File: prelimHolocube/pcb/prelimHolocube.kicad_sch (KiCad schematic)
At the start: 43 parts

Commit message: finish pcb
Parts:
- removed C15, C26, C28, C29, C30: 4.7uF, Capacitor_THT:CP_Radial_D4.0mm_P2.00mm, symbol Device:C_US
- removed C25, C27: 1uF, Capacitor_THT:CP_Radial_D5.0mm_P2.50mm, symbol Device:C
- removed R10: 1M, Resistor_THT:R_Axial_DIN0207_L6.3mm_D2.5mm_P7.62mm_Horizontal, symbol Device:R_US
- added C15, C7: 1uF, Capacitor_THT:CP_Radial_D5.0mm_P2.50mm, symbol Device:C
- added C16, C17, C18, C8, C9: 4.7uF, Capacitor_THT:CP_Radial_D4.0mm_P2.00mm, symbol Device:C_US
- added R6: 1M, Resistor_THT:R_Axial_DIN0207_L6.3mm_D2.5mm_P7.62mm_Horizontal, symbol Device:R_US
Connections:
- net +12V: now also C16.1, C8.1
- net +3.3V: now also C15.2, C7.2
- net A06: now also U7.4 (A0); no longer U6.4 (A0)
- net A07: now also U6.4 (A0); no longer U7.4 (A0)
- net CS6: now also U7.6 (CS); no longer U6.6 (CS)
- net CS7: now also U6.6 (CS); no longer U7.6 (CS)
- net GND: now also C15.1, C16.2, C17.2, C18.2, C7.1, C8.2, C9.2, R6.2
- net at C23.1: now also U7.10 (VCOMH); no longer U5.10 (VCOMH)
- net at U5.7 (IREF): now also R6.1; no longer R7.1
- net at R9.1: now also U8.7 (IREF); no longer U6.7 (IREF)
- net at U8.10 (VCOMH): now also C24.1
- net at U6.10 (VCOMH): now also C18.1
- net at U3.10 (VCOMH): now also C9.1; no longer C12.1
- net at U4.10 (VCOMH): now also C12.1
- new net: C17.1, U5.10 (VCOMH)
- new net: R7.1, U6.7 (IREF)

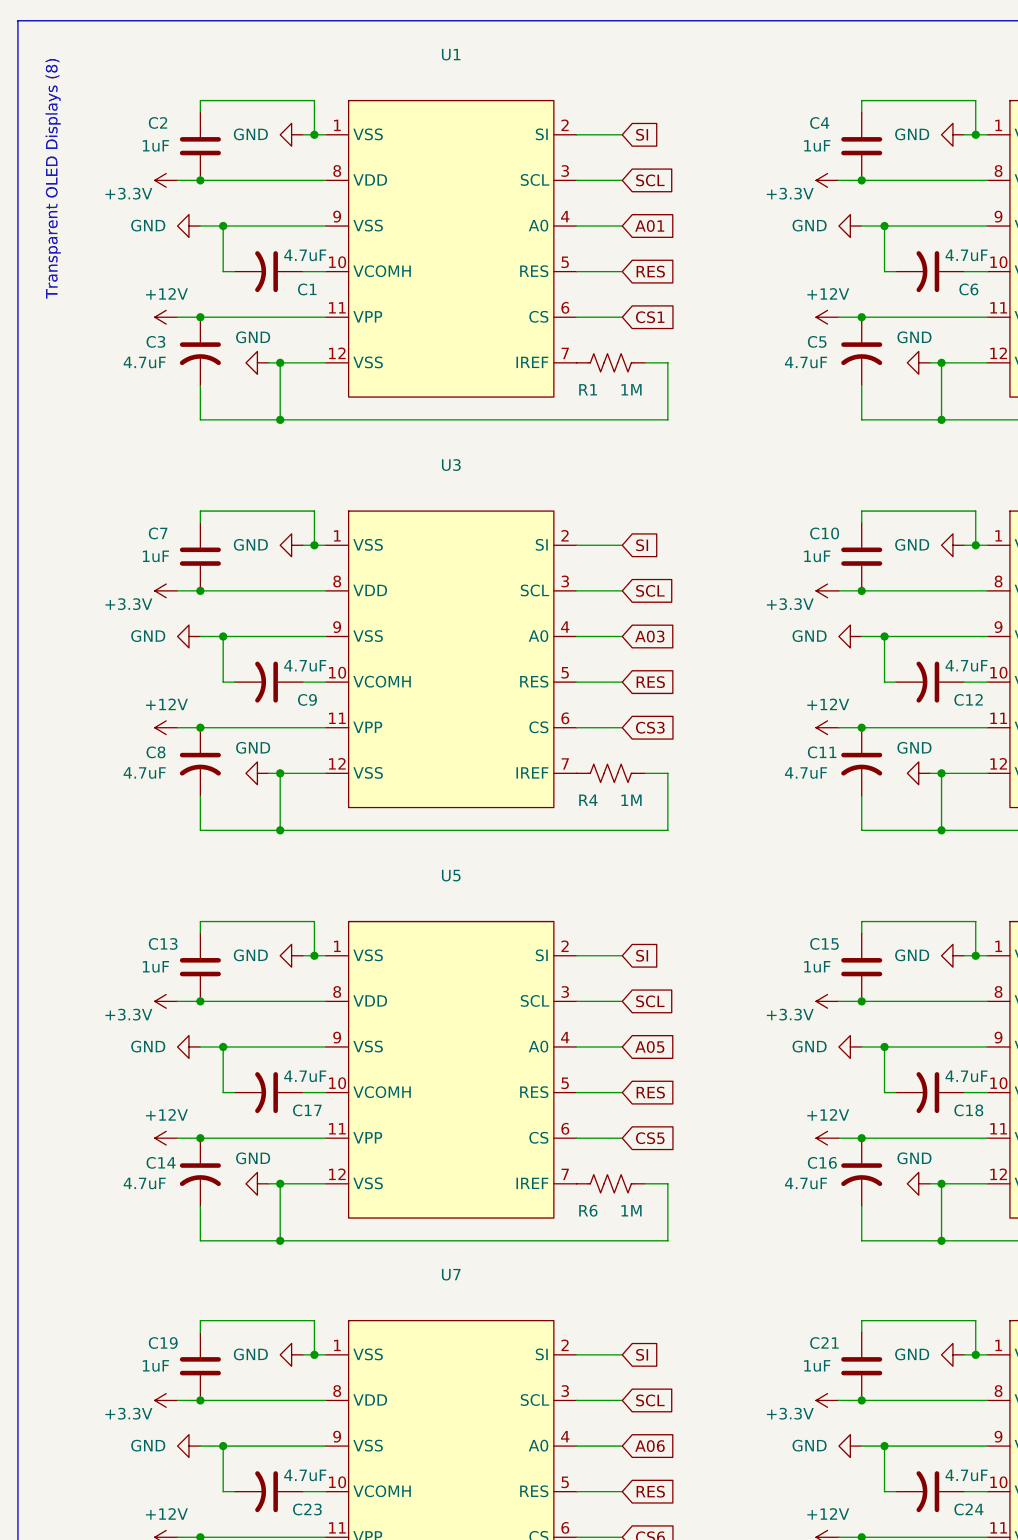
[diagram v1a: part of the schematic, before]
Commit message: switched to holo's prelimHolocube using this as a reference, deleted tracks to flip footprint, need to reroute
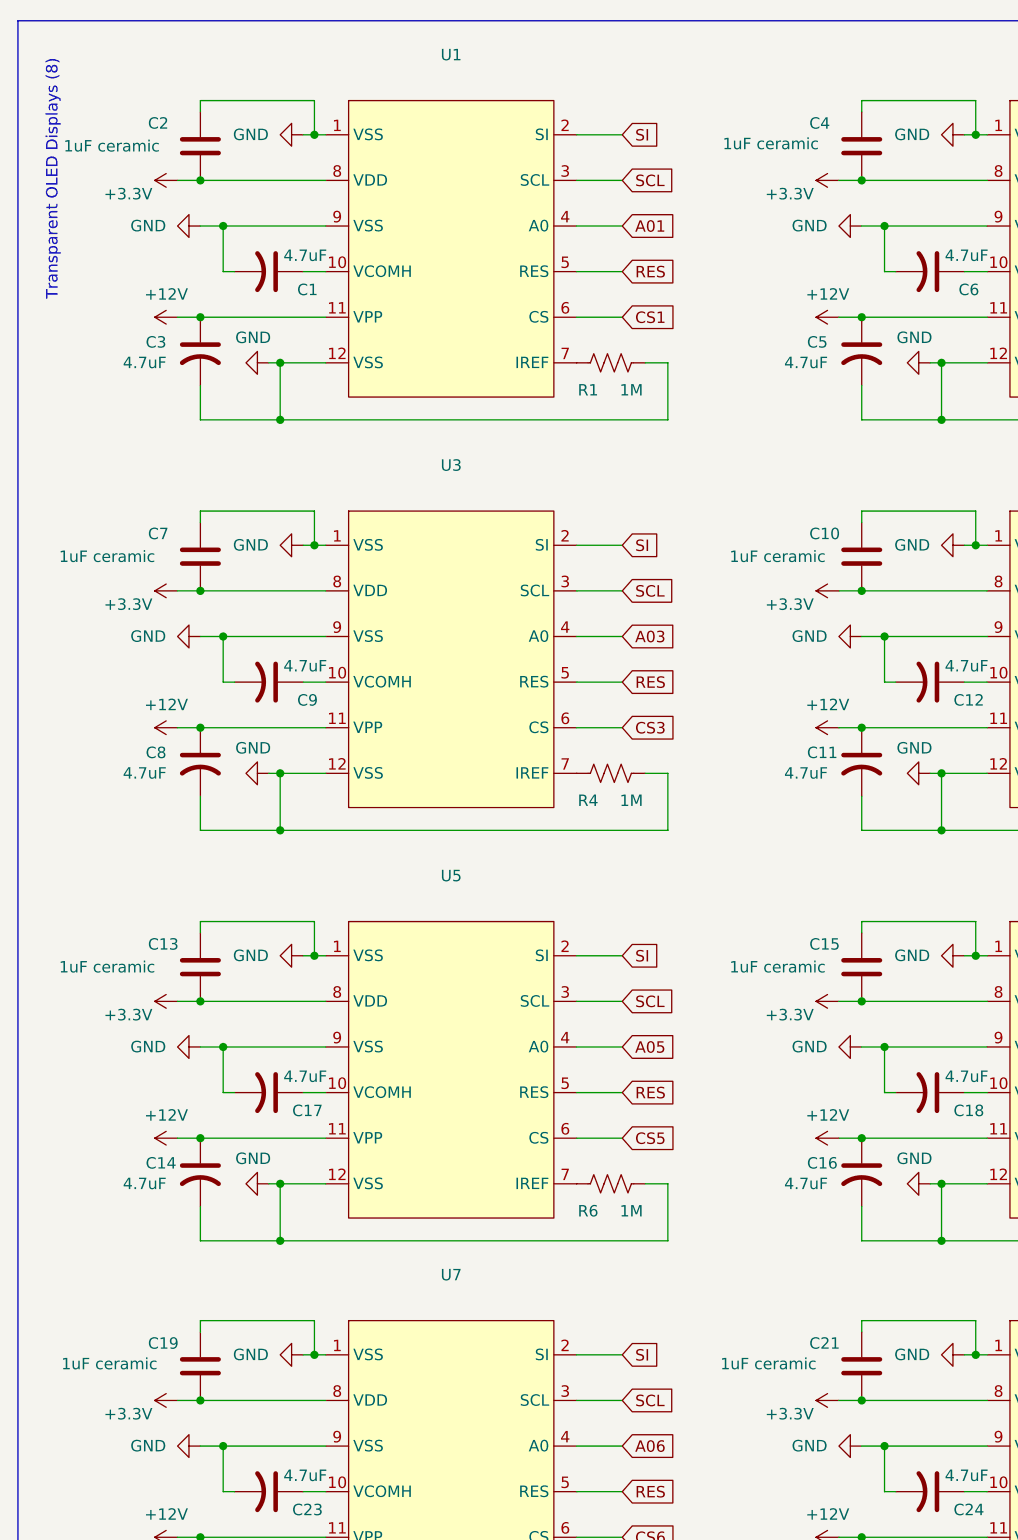
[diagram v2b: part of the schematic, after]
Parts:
- C10, C13, C15, C19, C2, C21, C4, C7: value 1uF -> 1uF ceramic
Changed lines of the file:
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@@
 			)
 		)
-		(property "Value" "1uF"
-			(at 26.416 118.11 0)
+		(property "Value" "1uF ceramic"
+			(at 17.272 118.11 0)
 			(effects
 				(font
@@
 			)
 		)
-		(property "Value" "1uF"
-			(at 26.416 162.56 0)
+		(property "Value" "1uF ceramic"
+			(at 17.526 162.306 0)
 			(effects
 				(font
@@
 			)
 		)
-		(property "Value" "1uF"
-			(at 26.416 26.67 0)
+		(property "Value" "1uF ceramic"
+			(at 17.78 26.67 0)
 			(effects
 				(font
@@
 			)
 		)
-		(property "Value" "1uF"
-			(at 26.416 72.39 0)
+		(property "Value" "1uF ceramic"
+			(at 17.272 72.39 0)
 			(effects
 				(font
@@
 			)
 		)
-		(property "Value" "1uF"
-			(at 100.076 72.39 0)
+		(property "Value" "1uF ceramic"
+			(at 91.948 72.39 0)
 			(effects
 				(font
@@
 			)
 		)
-		(property "Value" "1uF"
-			(at 100.076 118.11 0)
+		(property "Value" "1uF ceramic"
+			(at 91.948 118.11 0)
 			(effects
 				(font
@@
 			)
 		)
-		(property "Value" "1uF"
-			(at 100.076 26.67 0)
+		(property "Value" "1uF ceramic"
+			(at 91.186 26.416 0)
 			(effects
 				(font
@@
 			)
 		)
-		(property "Value" "1uF"
-			(at 100.076 162.56 0)
+		(property "Value" "1uF ceramic"
+			(at 90.932 162.306 0)
 			(effects
 				(font
